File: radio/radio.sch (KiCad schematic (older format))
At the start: 1 part

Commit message: 4-layer radio board
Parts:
- removed E1: ANT-433-SP, radio:XDCR_ANT-433-SP, symbol ANT-433-SP:ANT-433-SP
- added AE1: ANT-433-SP, star-common-lib:ANT-433-SP, symbol Device:Antenna_Chip
- added C1: 10uF, Capacitor_SMD:C_0603_1608Metric, symbol Device:C
- added C2, C9: 0.1uF, Capacitor_SMD:C_0603_1608Metric, symbol Device:C
- added C3, C4, C5: 1nF, Capacitor_SMD:C_0603_1608Metric, symbol Device:C
- added C6, C7: DNP, Capacitor_SMD:C_0603_1608Metric, symbol Device:C
- added C8: 1uF, Capacitor_SMD:C_0603_1608Metric, symbol Device:C
- added FB1, FB2: Ferrite_Bead, Inductor_SMD:L_0603_1608Metric, symbol Device:Ferrite_Bead
- added J1: SMA, star-common-lib:SMA_Molex_73391-0083_Horizontal, symbol Connector:Conn_Coaxial
- added L1: 0R, Inductor_SMD:L_0603_1608Metric, symbol Device:L
- added R1: 1k, Resistor_SMD:R_0603_1608Metric, symbol Device:R
- added U1: RFM69HCW, star-common-lib:RFM69HCW-XXXS2, symbol RF_Module:RFM69HCW
- added U2: 74AHC1G04, Package_TO_SOT_SMD:SOT-353_SC-70-5, symbol 74xGxx:74AHC1G04
- added U3: HMC544AE, Package_TO_SOT_SMD:SOT-23-6, symbol star-common-lib:HMC544AE
- added U4: ublox_SAM-M8Q, RF_GPS:ublox_SAM-M8Q, symbol RF_GPS:ublox_SAM-M8Q
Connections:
- net labels added: +3.3V, A, B, RF_INT, RF_RST, RF_Source, SCL, SDA
- net labels removed: IO_38, IO_39
- wire segments 23 -> 65
- no-connect marks 0 -> 11
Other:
- note added: "50 ohm impedance"
- note added: "A"
- note added: "Antenna & Switch"
- note added: "B"
- note added: "H"
- note added: "L"
- note added: "Mode"
- note added: "RFC -> RF1"
- note added: "RFC -> RF2"
- note added: "Radio Module"
- note removed: "Antenna"
- note removed: "Radio"

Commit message: Added solder jumper to select source, removed radio INT
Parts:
- added JP1: Default_Source, Jumper:SolderJumper-3_P1.3mm_Bridged12_RoundedPad1.0x1.5mm, symbol Jumper:Jumper_3_Bridged12
- added JP2: Jumper, Jumper:SolderJumper-2_P1.3mm_Bridged_RoundedPad1.0x1.5mm, symbol Device:Jumper
- added R2: 1k, Resistor_SMD:R_0603_1608Metric, symbol Device:R
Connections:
- net +3V3: now also JP1.3 (B)
- net A: now also JP2.2
- net GND: now also R2.1; no longer R1.2
- net RF_INT: no longer names the net of U1.14 (DIO0)
- new net: JP1.2 (C), R1.2
- new net: JP1.1 (A), R2.2
- new net RF_Source: JP2.1
- no-connect marks 11 -> 12
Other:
- note added: ""RF_Source" connects to GPIO on MCU. \nMCU control takes priority over JP1 selection.\nMCU connection can be disconnected using JP2."
- note added: "GNSS Module"
- moved on the sheet: AE1, C3, C4, C5, C6, C7, C8, C9, FB1, FB2, J1, L1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

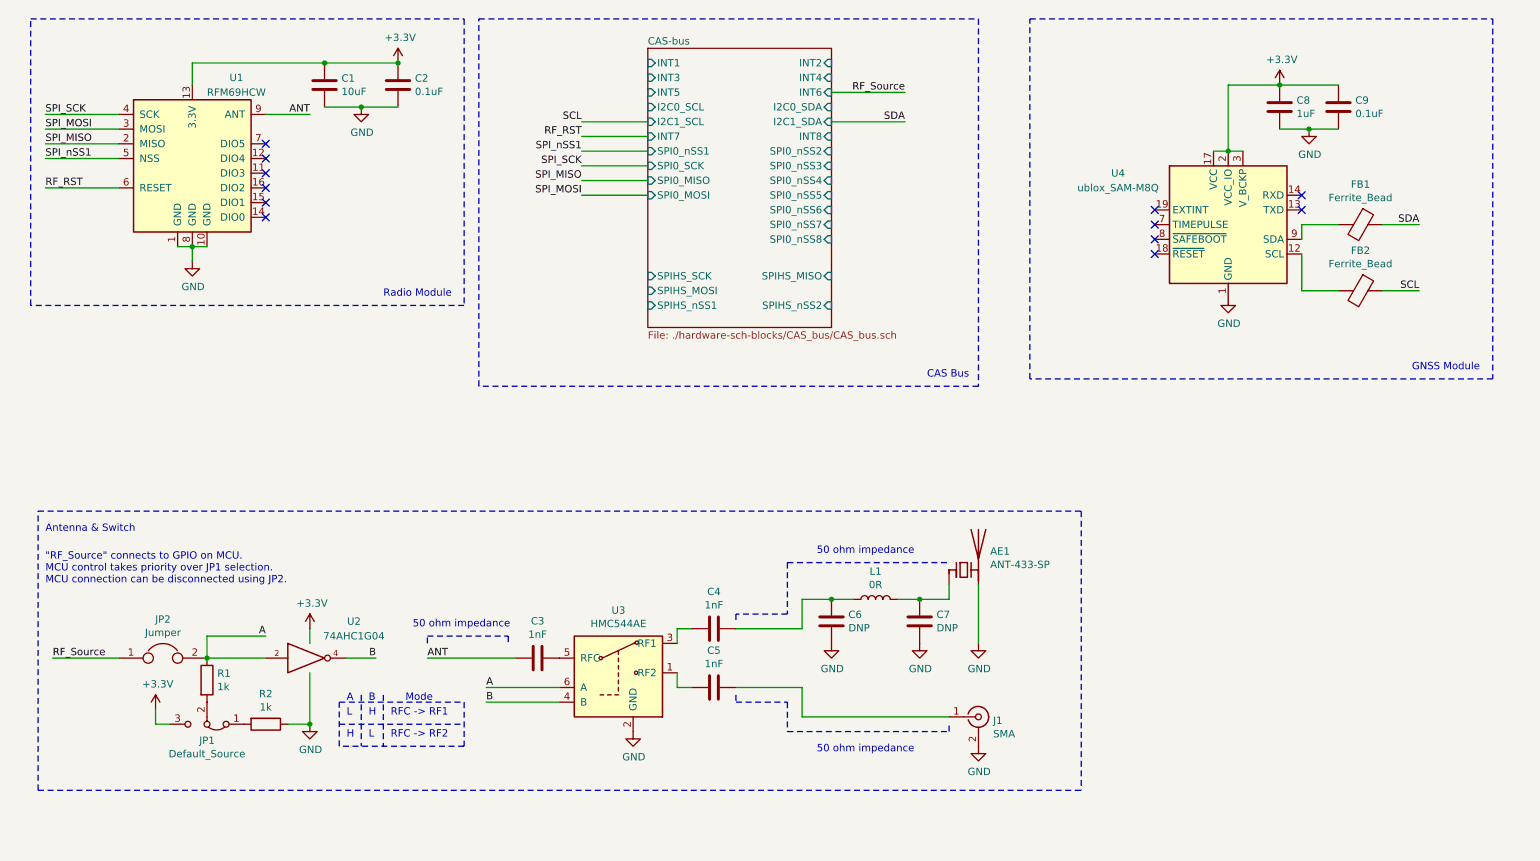
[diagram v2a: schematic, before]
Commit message: Add test pins
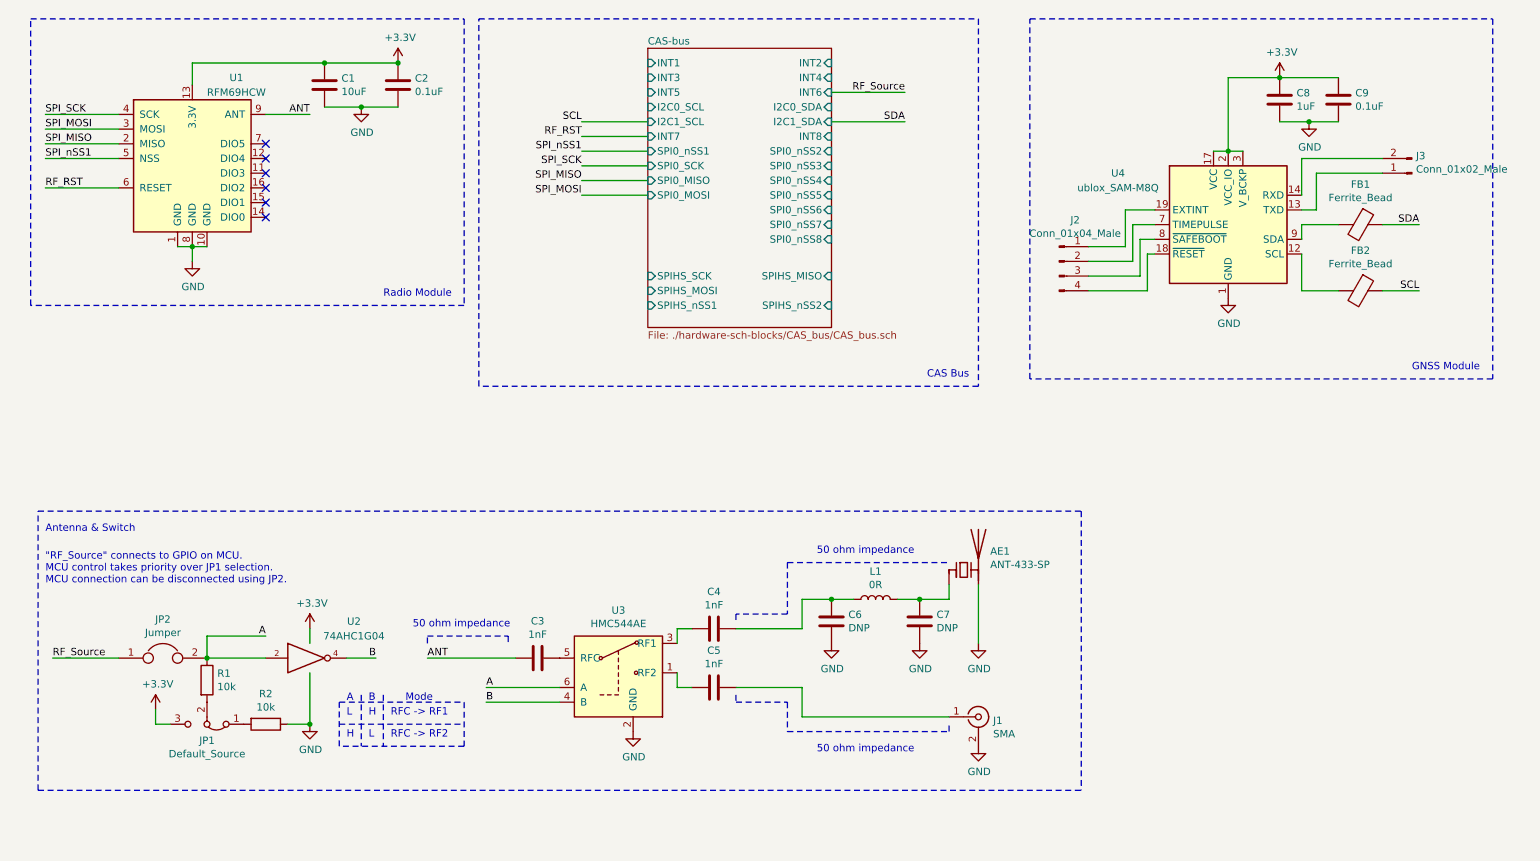
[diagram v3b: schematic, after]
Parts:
- added J2: Conn_01x04_Male, Connector_PinHeader_2.54mm:PinHeader_1x04_P2.54mm_Vertical_SMD_Pin1Left, symbol Connector:Conn_01x04_Male
- added J3: Conn_01x02_Male, Connector_PinHeader_2.54mm:PinHeader_1x02_P2.54mm_Vertical_SMD_Pin1Left, symbol Connector:Conn_01x02_Male
- R1, R2: value 1k -> 10k
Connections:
- net at U4.13 (TXD): now also J3.1 (Pin_1)
- net at U4.14 (RXD): now also J3.2 (Pin_2)
- net at U4.18 (~RESET): now also J2.4 (Pin_4)
- net at U4.19 (EXTINT): now also J2.1 (Pin_1)
- net at U4.7 (TIMEPULSE): now also J2.2 (Pin_2)
- net at U4.8 (~SAFEBOOT): now also J2.3 (Pin_3)
- no-connect marks 12 -> 6
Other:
- moved on the sheet: C8, C9
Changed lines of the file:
@@
 P 1850 5100
 F 0 "R1" H 1920 5146 50  0000 L CNN
-F 1 "1k" H 1920 5055 50  0000 L CNN
+F 1 "10k" H 1920 5055 50  0000 L CNN
 F 2 "Resistor_SMD:R_0603_1608Metric" V 1780 5100 50  0001 C CNN
 F 3 "~" H 1850 5100 50  0001 C CNN
@@
 Text Label 10100 2450 2    50   ~ 0
 SCL
-NoConn ~ 8300 2200
-NoConn ~ 8300 2100
-NoConn ~ 8300 2000
-NoConn ~ 8300 1900
 Wire Wire Line
 	8700 1500 8800 1500
@@
 L power:+3.3V #PWR041
 U 1 1 5FF2B3BE
-P 9150 1050
-F 0 "#PWR041" H 9150 900 50  0001 C CNN
-F 1 "+3.3V" H 9165 1223 50  0000 C CNN
-F 2 "" H 9150 1050 50  0001 C CNN
-F 3 "" H 9150 1050 50  0001 C CNN
-	1    9150 1050
-	1    0    0    -1
-$EndComp
-NoConn ~ 9300 1800
-NoConn ~ 9300 1900
+P 9150 1000
+F 0 "#PWR041" H 9150 850 50  0001 C CNN
+F 1 "+3.3V" H 9165 1173 50  0000 C CNN
+F 2 "" H 9150 1000 50  0001 C CNN
+F 3 "" H 9150 1000 50  0001 C CNN
+	1    9150 1000
+	1    0    0    -1
+$EndComp
 $Comp
 L Device:Ferrite_Bead FB1
@@
 L Device:C C8
 U 1 1 5FF76E3F
-P 9150 1200
-F 0 "C8" H 9265 1246 50  0000 L CNN
-F 1 "1uF" H 9265 1155 50  0000 L CNN
-F 2 "Capacitor_SMD:C_0603_1608Metric" H 9188 1050 50  0001 C CNN
-F 3 "~" H 9150 1200 50  0001 C CNN
-	1    9150 1200
+P 9150 1150
+F 0 "C8" H 9265 1196 50  0000 L CNN
+F 1 "1uF" H 9265 1105 50  0000 L CNN
+F 2 "Capacitor_SMD:C_0603_1608Metric" H 9188 1000 50  0001 C CNN
+F 3 "~" H 9150 1150 50  0001 C CNN
+	1    9150 1150
 	1    0    0    -1
 $EndComp
@@
 L Device:C C9
 U 1 1 5FF773AF
-P 9550 1200
-F 0 "C9" H 9665 1246 50  0000 L CNN
-F 1 "0.1uF" H 9665 1155 50  0000 L CNN
-F 2 "Capacitor_SMD:C_0603_1608Metric" H 9588 1050 50  0001 C CNN
-F 3 "~" H 9550 1200 50  0001 C CNN
-	1    9550 1200
+P 9550 1150
+F 0 "C9" H 9665 1196 50  0000 L CNN
+F 1 "0.1uF" H 9665 1105 50  0000 L CNN
+F 2 "Capacitor_SMD:C_0603_1608Metric" H 9588 1000 50  0001 C CNN
+F 3 "~" H 9550 1150 50  0001 C CNN
+	1    9550 1150
 	1    0    0    -1
 $EndComp
@@
 L power:GND #PWR042
 U 1 1 5FF793DE
-P 9350 1350
-F 0 "#PWR042" H 9350 1100 50  0001 C CNN
-F 1 "GND" H 9355 1177 50  0000 C CNN
-F 2 "" H 9350 1350 50  0001 C CNN
-F 3 "" H 9350 1350 50  0001 C CNN
-	1    9350 1350
-	1    0    0    -1
-$EndComp
-Wire Wire Line
-	9150 1350 9350 1350
-Connection ~ 9350 1350
-Wire Wire Line
-	9350 1350 9550 1350
-Wire Wire Line
-	9550 1050 9150 1050
-Connection ~ 9150 1050
-Wire Wire Line
-	9150 1050 8800 1050
-Wire Wire Line
-	8800 1050 8800 1500
+P 9350 1300
+F 0 "#PWR042" H 9350 1050 50  0001 C CNN
+F 1 "GND" H 9355 1127 50  0000 C CNN
+F 2 "" H 9350 1300 50  0001 C CNN
+F 3 "" H 9350 1300 50  0001 C CNN
+	1    9350 1300
+	1    0    0    -1
+$EndComp
+Wire Wire Line
+	9150 1300 9350 1300
+Connection ~ 9350 1300
+Wire Wire Line
+	9350 1300 9550 1300
+Wire Wire Line
+	9550 1000 9150 1000
+Connection ~ 9150 1000
+Wire Wire Line
+	9150 1000 8800 1000
 Wire Wire Line
 	800  4950 1250 4950
@@
 P 2250 5400
 F 0 "R2" V 2043 5400 50  0000 C CNN
-F 1 "1k" V 2134 5400 50  0000 C CNN
+F 1 "10k" V 2134 5400 50  0000 C CNN
 F 2 "Resistor_SMD:R_0603_1608Metric" V 2180 5400 50  0001 C CNN
 F 3 "~" H 2250 5400 50  0001 C CNN
@@
 Wire Wire Line
 	1850 4800 2250 4800
+$Comp
+L Connector:Conn_01x02_Male J3
+U 1 1 5FFD14F8
+P 10050 1650
+F 0 "J3" H 10022 1532 50  0000 R CNN
+F 1 "Conn_01x02_Male" H 10022 1623 50  0000 R CNN
+F 2 "Connector_PinHeader_2.54mm:PinHeader_1x02_P2.54mm_Vertical_SMD_Pin1Left" H 10050 1650 50  0001 C CNN
+F 3 "~" H 10050 1650 50  0001 C CNN
+	1    10050 1650
+	-1   0    0    1
+$EndComp
+Wire Wire Line
+	9300 1550 9850 1550
+Wire Wire Line
+	9300 1900 9400 1900
+Wire Wire Line
+	9400 1650 9400 1900
+Wire Wire Line
+	9400 1650 9850 1650
+$Comp
+L Connector:Conn_01x04_Male J2
+U 1 1 5FFDF6A0
+P 7650 2250
+F 0 "J2" H 7758 2531 50  0000 C CNN
+F 1 "Conn_01x04_Male" H 7758 2440 50  0000 C CNN
+F 2 "Connector_PinHeader_2.54mm:PinHeader_1x04_P2.54mm_Vertical_SMD_Pin1Left" H 7650 2250 50  0001 C CNN
+F 3 "~" H 7650 2250 50  0001 C CNN
+	1    7650 2250
+	1    0    0    -1
+$EndComp
+Wire Wire Line
+	8100 1900 8100 2150
+Wire Wire Line
+	7850 2150 8100 2150
+Wire Wire Line
+	8150 2000 8150 2250
+Wire Wire Line
+	7850 2250 8150 2250
+Wire Wire Line
+	7850 2350 8200 2350
+Wire Wire Line
+	7850 2450 8250 2450
+Wire Wire Line
+	8150 2000 8300 2000
+Wire Wire Line
+	8200 2100 8200 2350
+Wire Wire Line
+	8200 2100 8300 2100
+Wire Wire Line
+	8300 2200 8250 2200
+Wire Wire Line
+	8250 2200 8250 2450
+Wire Wire Line
+	9300 1800 9300 1550
+Wire Wire Line
+	8800 1000 8800 1500
+Wire Wire Line
+	8100 1900 8300 1900
 $EndSCHEMATC

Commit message: Added digikey part numbers
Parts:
- AE1: Digikey P/N (none) -> ANT-433-SP-ND
- C1: Digikey P/N (none) -> 490-13248-1-ND
- C2, C9: Digikey P/N (none) -> 399-1100-1-ND
- C3, C4, C5: Digikey P/N (none) -> 1276-1091-1-ND
- C8: Digikey P/N (none) -> 1276-1102-1-ND
- FB1, FB2: Digikey P/N (none) -> 587-1879-1-ND
- J1: Digikey P/N (none) -> WM4088-ND
- J2: Digikey P/N (none) -> 609-10129380-904002ALFCT-ND
- J3: Digikey P/N (none) -> 609-10129380-902001BLF-ND
- L1: Digikey P/N (none) -> 311-0.0HRCT-ND
- R1, R2: Digikey P/N (none) -> 311-10KGRCT-ND
- U1: Digikey P/N (none) -> 1568-1391-ND
- U2: Digikey P/N (none) -> 74AHC1G04SE-7DICT-ND
- U3: Digikey P/N (none) -> 1127-3205-ND
- U4: Digikey P/N (none) -> 672-1054-6-ND
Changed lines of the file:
@@
 F 2 "star-common-lib:RFM69HCW-XXXS2" H -1550 3200 50  0001 C CNN
 F 3 "https://www.hoperf.com/data/upload/portal/20181127/5bfcb8284d838.pdf" H -1550 3200 50  0001 C CNN
+F 4 "1568-1391-ND" H 1750 1550 50  0001 C CNN "Digikey P/N"
 	1    1750 1550
 	1    0    0    -1
@@
 F 2 "Capacitor_SMD:C_0603_1608Metric" H 2688 900 50  0001 C CNN
 F 3 "~" H 2650 1050 50  0001 C CNN
+F 4 "490-13248-1-ND" H 2650 1050 50  0001 C CNN "Digikey P/N"
 	1    2650 1050
 	1    0    0    -1
@@
 F 2 "Capacitor_SMD:C_0603_1608Metric" H 3188 900 50  0001 C CNN
 F 3 "~" H 3150 1050 50  0001 C CNN
+F 4 "399-1100-1-ND" H 3150 1050 50  0001 C CNN "Digikey P/N"
 	1    3150 1050
 	1    0    0    -1
@@
 F 2 "star-common-lib:ANT-433-SP" H 6900 4525 50  0001 C CNN
 F 3 "~" H 6900 4525 50  0001 C CNN
+F 4 "ANT-433-SP-ND" H 7000 4350 50  0001 C CNN "Digikey P/N"
 	1    7000 4350
 	1    0    0    -1
@@
 F 2 "Inductor_SMD:L_0603_1608Metric" H 6400 4550 50  0001 C CNN
 F 3 "~" H 6400 4550 50  0001 C CNN
+F 4 "311-0.0HRCT-ND" H 6400 4550 50  0001 C CNN "Digikey P/N"
 	1    6400 4550
 	0    -1   -1   0
@@
 F 2 "star-common-lib:SMA_Molex_73391-0083_Horizontal" H 7100 5350 50  0001 C CNN
 F 3 " ~" H 7100 5350 50  0001 C CNN
+F 4 "WM4088-ND" H 7100 5350 50  0001 C CNN "Digikey P/N"
 	1    7100 5350
 	1    0    0    -1
@@
 F 2 "Package_TO_SOT_SMD:SOT-23-6" H 4650 5350 50  0001 C CNN
 F 3 "https://www.analog.com/media/en/technical-documentation/data-sheets/hmc544ae.pdf" H 4650 5050 50  0001 C CNN
+F 4 "1127-3205-ND" H 4650 5050 50  0001 C CNN "Digikey P/N"
 	1    4650 5050
 	1    0    0    -1
@@
 F 2 "Package_TO_SOT_SMD:SOT-353_SC-70-5" H 2550 4950 50  0001 C CNN
 F 3 "http://www.ti.com/lit/sg/scyt129e/scyt129e.pdf" H 2550 4950 50  0001 C CNN
+F 4 "74AHC1G04SE-7DICT-ND" H 2550 4950 50  0001 C CNN "Digikey P/N"
 	1    2550 4950
 	1    0    0    -1
@@
 F 2 "Resistor_SMD:R_0603_1608Metric" V 1780 5100 50  0001 C CNN
 F 3 "~" H 1850 5100 50  0001 C CNN
+F 4 "311-10KGRCT-ND" H 1850 5100 50  0001 C CNN "Digikey P/N"
 	1    1850 5100
 	1    0    0    -1
@@
 F 2 "Capacitor_SMD:C_0603_1608Metric" H 4138 4800 50  0001 C CNN
 F 3 "~" H 4100 4950 50  0001 C CNN
+F 4 "1276-1091-1-ND" H 4100 4950 50  0001 C CNN "Digikey P/N"
 	1    4100 4950
 	0    1    1    0
@@
 F 2 "Capacitor_SMD:C_0603_1608Metric" H 5338 4600 50  0001 C CNN
 F 3 "~" H 5300 4750 50  0001 C CNN
+F 4 "1276-1091-1-ND" H 5300 4750 50  0001 C CNN "Digikey P/N"
 	1    5300 4750
 	0    1    1    0
@@
 F 2 "Capacitor_SMD:C_0603_1608Metric" H 5338 5000 50  0001 C CNN
 F 3 "~" H 5300 5150 50  0001 C CNN
+F 4 "1276-1091-1-ND" H 5300 5150 50  0001 C CNN "Digikey P/N"
 	1    5300 5150
 	0    1    1    0
@@
 F 2 "RF_GPS:ublox_SAM-M8Q" H 9300 1550 50  0001 C CNN
 F 3 "https://www.u-blox.com/sites/default/files/SAM-M8Q_DataSheet_%28UBX-16012619%29.pdf" H 8800 2000 50  0001 C CNN
+F 4 "672-1054-6-ND" H 8800 2000 50  0001 C CNN "Digikey P/N"
 	1    8800 2000
 	1    0    0    -1
@@
 F 2 "Inductor_SMD:L_0603_1608Metric" V 9630 2000 50  0001 C CNN
 F 3 "~" H 9700 2000 50  0001 C CNN
+F 4 "587-1879-1-ND" H 9700 2000 50  0001 C CNN "Digikey P/N"
 	1    9700 2000
 	0    1    1    0
@@
 F 2 "Inductor_SMD:L_0603_1608Metric" V 9630 2450 50  0001 C CNN
 F 3 "~" H 9700 2450 50  0001 C CNN
+F 4 "587-1879-1-ND" H 9700 2450 50  0001 C CNN "Digikey P/N"
 	1    9700 2450
 	0    1    1    0
@@
 F 2 "Capacitor_SMD:C_0603_1608Metric" H 9188 1000 50  0001 C CNN
 F 3 "~" H 9150 1150 50  0001 C CNN
+F 4 "1276-1102-1-ND" H 9150 1150 50  0001 C CNN "Digikey P/N"
 	1    9150 1150
 	1    0    0    -1
@@
 F 2 "Capacitor_SMD:C_0603_1608Metric" H 9588 1000 50  0001 C CNN
 F 3 "~" H 9550 1150 50  0001 C CNN
+F 4 "399-1100-1-ND" H 9550 1150 50  0001 C CNN "Digikey P/N"
 	1    9550 1150
 	1    0    0    -1
@@
 F 2 "Resistor_SMD:R_0603_1608Metric" V 2180 5400 50  0001 C CNN
 F 3 "~" H 2250 5400 50  0001 C CNN
+F 4 "311-10KGRCT-ND" H 2250 5400 50  0001 C CNN "Digikey P/N"
 	1    2250 5400
 	0    1    1    0
@@
 F 2 "Connector_PinHeader_2.54mm:PinHeader_1x02_P2.54mm_Vertical_SMD_Pin1Left" H 10050 1650 50  0001 C CNN
 F 3 "~" H 10050 1650 50  0001 C CNN
+F 4 "609-10129380-902001BLF-ND" H 10050 1650 50  0001 C CNN "Digikey P/N"
 	1    10050 1650
 	-1   0    0    1
@@
 F 2 "Connector_PinHeader_2.54mm:PinHeader_1x04_P2.54mm_Vertical_SMD_Pin1Left" H 7650 2250 50  0001 C CNN
 F 3 "~" H 7650 2250 50  0001 C CNN
+F 4 "609-10129380-904002ALFCT-ND" H 7650 2250 50  0001 C CNN "Digikey P/N"
 	1    7650 2250
 	1    0    0    -1
